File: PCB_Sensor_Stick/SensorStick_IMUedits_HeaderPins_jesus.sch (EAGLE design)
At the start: 48 parts, among them IC1 SAM-M8Q-0-10, IC2 STM32L412RBT6P, IC3 DPS310XTSA1, IC5 BMI085, IC6 IIS2MDCTR, J1 USB4160-03-0230-C, U1 4525DO-DS5AI001DP, U2 LD39050PU33R

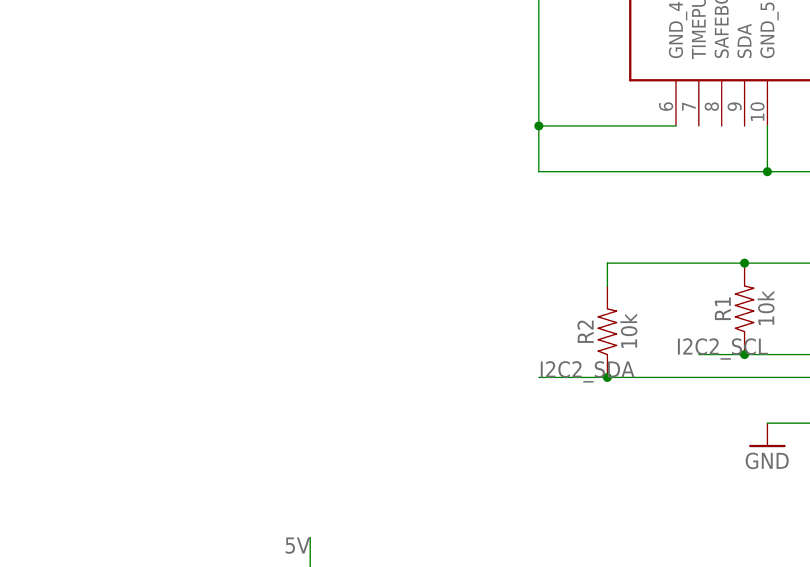
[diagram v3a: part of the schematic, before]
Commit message: J - Added header pins for remaining I2C lines
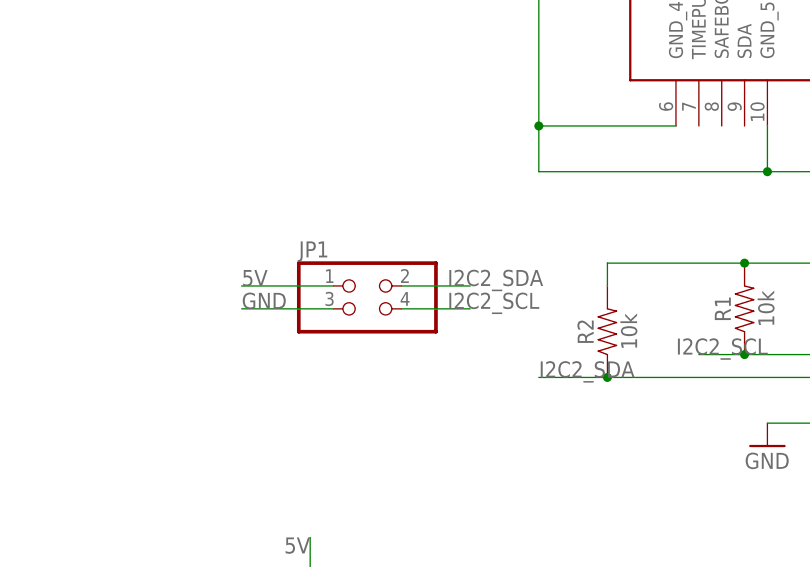
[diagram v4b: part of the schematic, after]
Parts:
- added JP1: (no value), pinhead:PINHD-2X2
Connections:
- net 5V: now also JP1.1
- net GND: now also JP1.3
- net I2C2_SCL: now also JP1.4
- net I2C2_SDA: now also JP1.2
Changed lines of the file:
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@@
 <part name="JP5" library="pinhead" library_urn="urn:adsk.eagle:library:325" deviceset="PINHD-2X3" device="" package3d_urn="urn:adsk.eagle:package:22462/2"/>
 <part name="JP2" library="pinhead" library_urn="urn:adsk.eagle:library:325" deviceset="PINHD-2X2" device="" package3d_urn="urn:adsk.eagle:package:22455/2"/>
+<part name="JP1" library="pinhead" library_urn="urn:adsk.eagle:library:325" deviceset="PINHD-2X2" device="" package3d_urn="urn:adsk.eagle:package:22455/2"/>
 </parts>
 <sheets>
@@
 <attribute name="NAME" x="3.81" y="-62.865" size="1.778" layer="95"/>
 <attribute name="VALUE" x="3.81" y="-73.66" size="1.778" layer="96"/>
+</instance>
+<instance part="JP1" gate="A" x="-17.78" y="2.54" smashed="yes">
+<attribute name="NAME" x="-26.67" y="8.255" size="1.778" layer="95"/>
+<attribute name="VALUE" x="-26.67" y="-2.54" size="1.778" layer="96"/>
 </instance>
 </instances>
@@
 <label x="264.16" y="-35.56" size="1.778" layer="95"/>
 </segment>
+<segment>
+<pinref part="JP1" gate="A" pin="3"/>
+<wire x1="-22.86" y1="2.54" x2="-33.02" y2="2.54" width="0.1524" layer="91"/>
+<label x="-33.02" y="2.54" size="1.778" layer="95"/>
+</segment>
 </net>
 <net name="TX" class="0">
@@
 <wire x1="129.54" y1="5.08" x2="129.54" y2="-10.16" width="0.1524" layer="91"/>
 <label x="129.54" y="-10.16" size="1.778" layer="95" rot="R90"/>
+</segment>
+<segment>
+<pinref part="JP1" gate="A" pin="4"/>
+<wire x1="-15.24" y1="2.54" x2="-7.62" y2="2.54" width="0.1524" layer="91"/>
+<label x="-10.16" y="2.54" size="1.778" layer="95"/>
 </segment>
 </net>
@@
 <wire x1="132.08" y1="5.08" x2="132.08" y2="-10.16" width="0.1524" layer="91"/>
 <label x="132.08" y="-10.16" size="1.778" layer="95" rot="R90"/>
+</segment>
+<segment>
+<pinref part="JP1" gate="A" pin="2"/>
+<wire x1="-15.24" y1="5.08" x2="-7.62" y2="5.08" width="0.1524" layer="91"/>
+<label x="-10.16" y="5.08" size="1.778" layer="95"/>
 </segment>
 </net>
@@
 <label x="-25.4" y="-22.86" size="1.778" layer="95" rot="R180"/>
 </segment>
-</net>
+<segment>
+<pinref part="JP1" gate="A" pin="1"/>
+<wire x1="-22.86" y1="5.08" x2="-33.02" y2="5.08" width="0.1524" layer="91"/>
+<label x="-33.02" y="5.08" size="1.778" layer="95"/>
+</segment>
+</net>

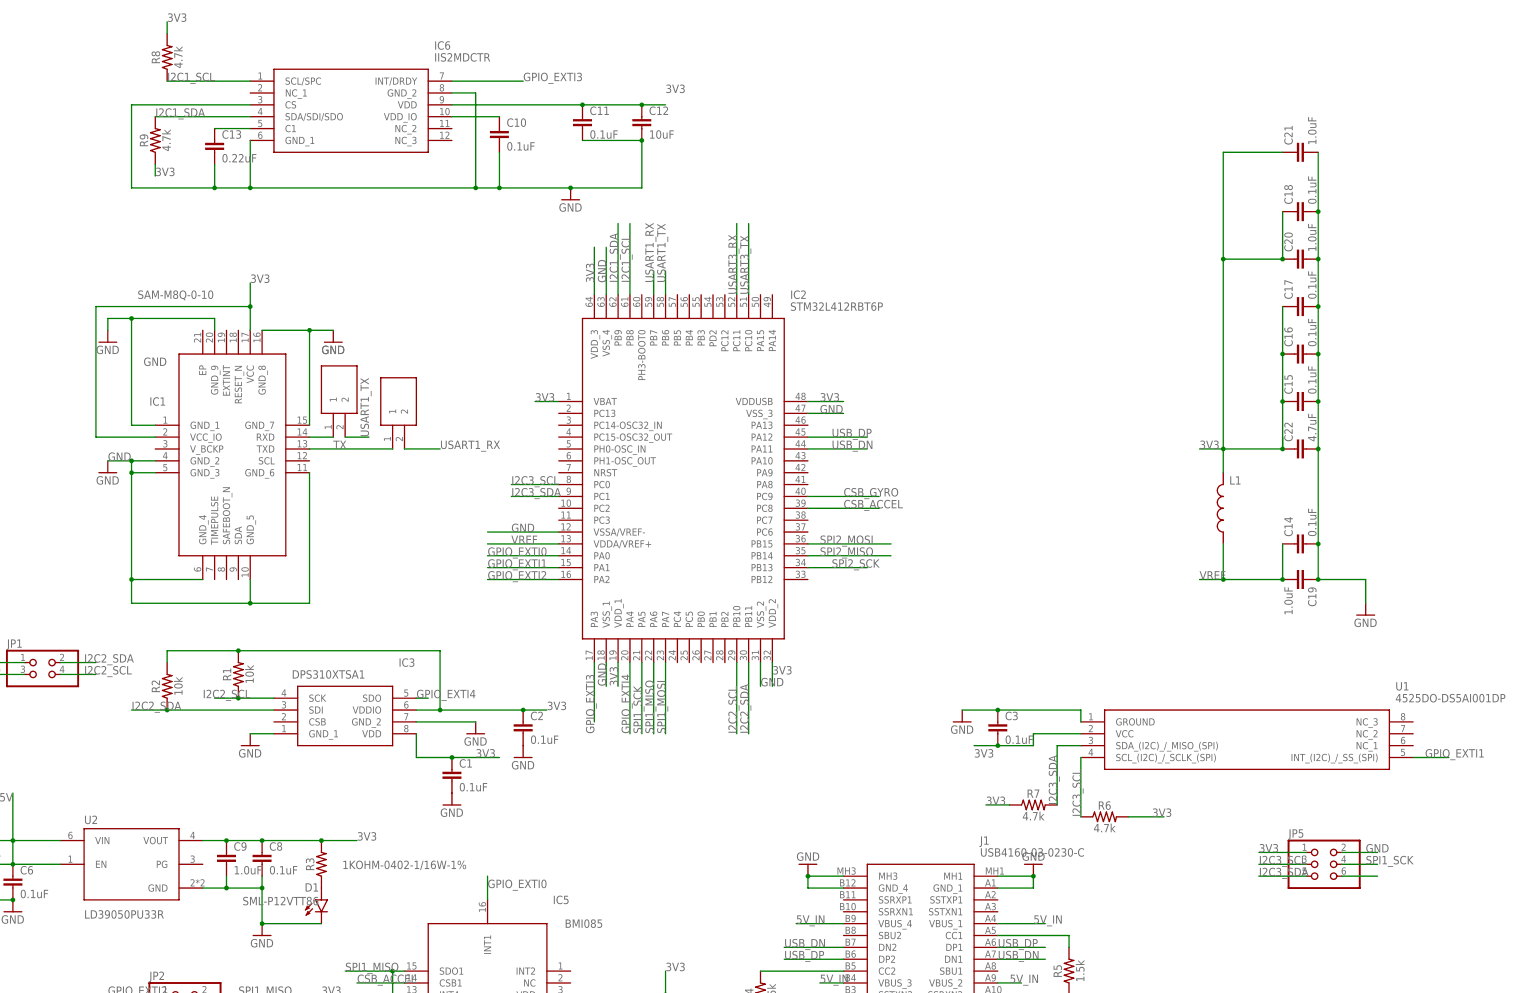
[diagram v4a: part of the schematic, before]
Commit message: Added in JST connection and renamed all sensors
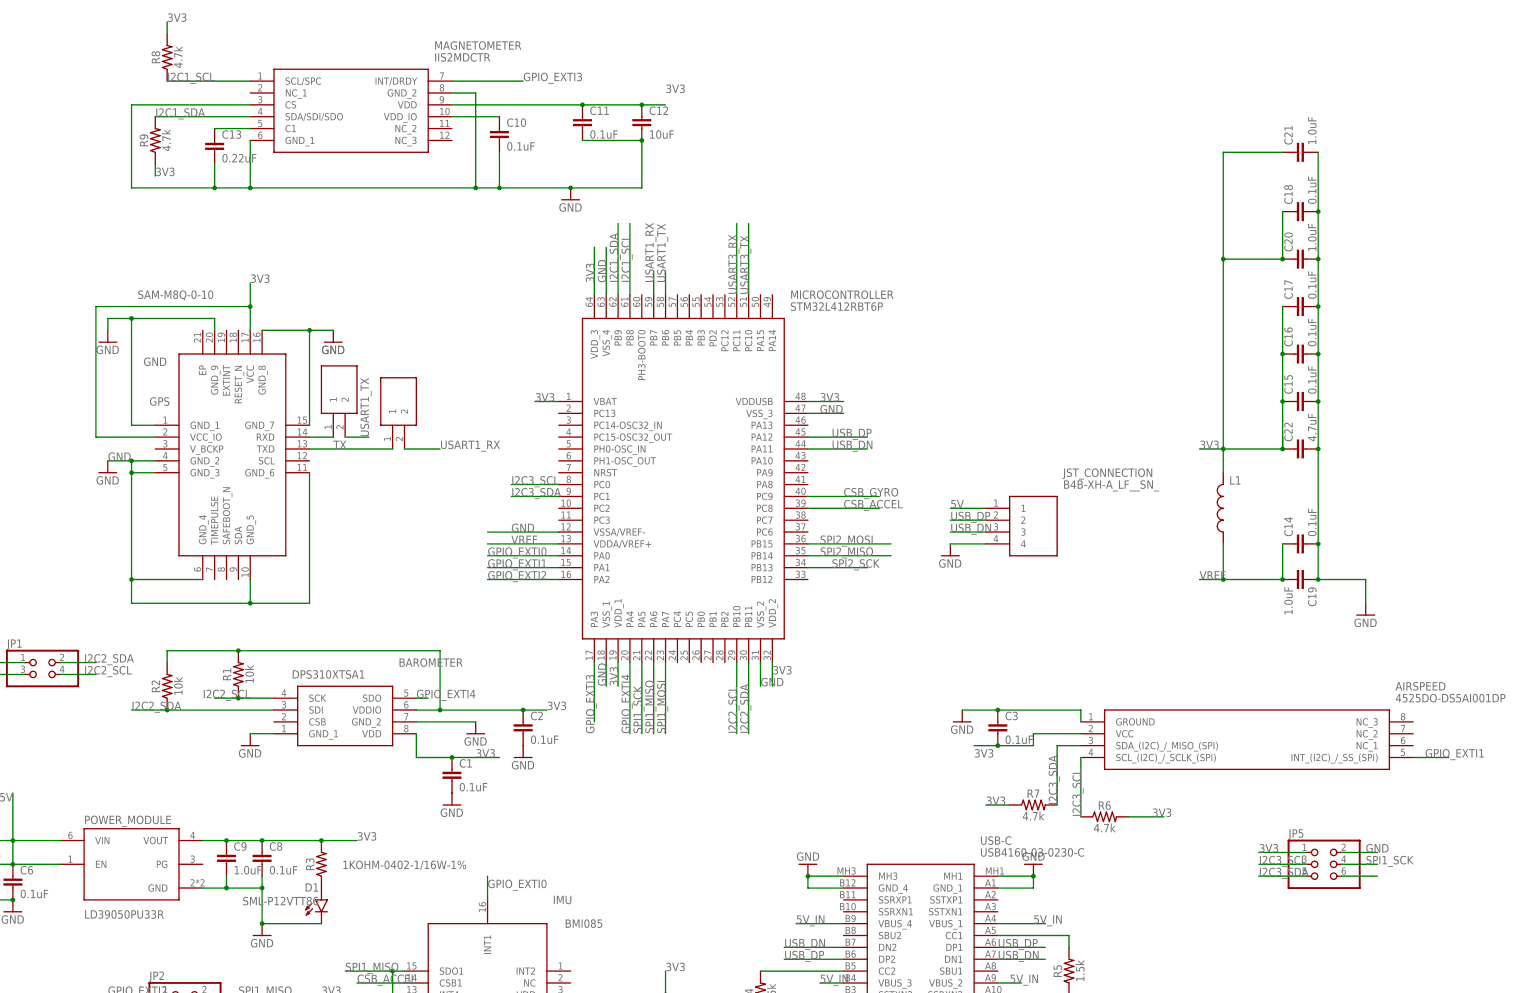
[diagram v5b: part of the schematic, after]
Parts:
- added JST_CONNECTION: B4B-XH-A_LF__SN_, B4B-XH-A_LF__SN_:B4B-XH-A_LF__SN_
- renumbered IC1 to GPS, IC2 to MICROCONTROLLER, IC3 to BAROMETER, IC5 to IMU, IC6 to MAGNETOMETER, J1 to USB-C, U1 to AIRSPEED, U2 to POWER_MODULE
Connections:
- net 5V: now also JST_CONNECTION.1
- net GND: now also JST_CONNECTION.4
- net USB_DN: now also JST_CONNECTION.3
- net USB_DP: now also JST_CONNECTION.2
